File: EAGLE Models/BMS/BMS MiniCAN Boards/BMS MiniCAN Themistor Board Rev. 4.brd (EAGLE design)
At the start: 150.2 x 63.2 mm, 112 parts, among them IC1 AT90CAN128, IC2 MCP2551SO8, IC3 NUP2105L, U1 0ZCH0050FF2G

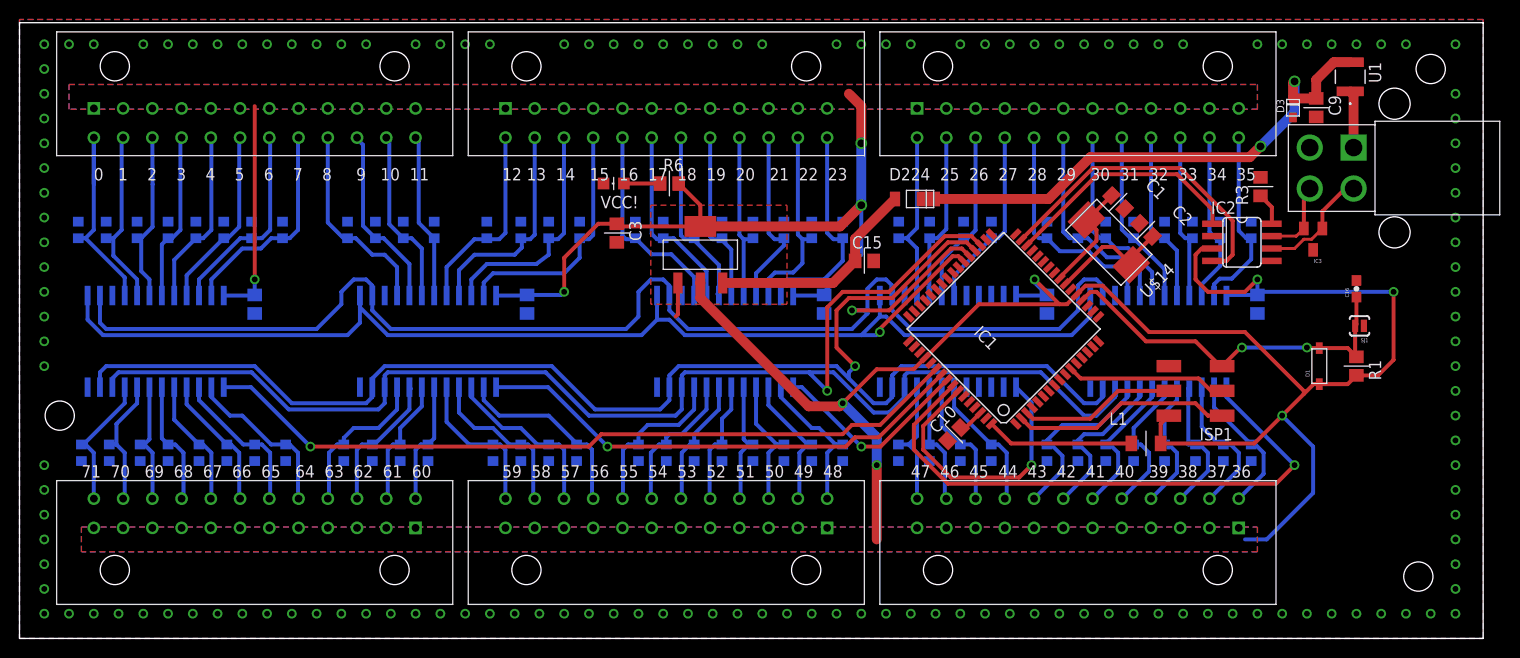
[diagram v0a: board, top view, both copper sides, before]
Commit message: Fixed silkscreens and crystal
Fixed the silkscreens and replaced crystal.
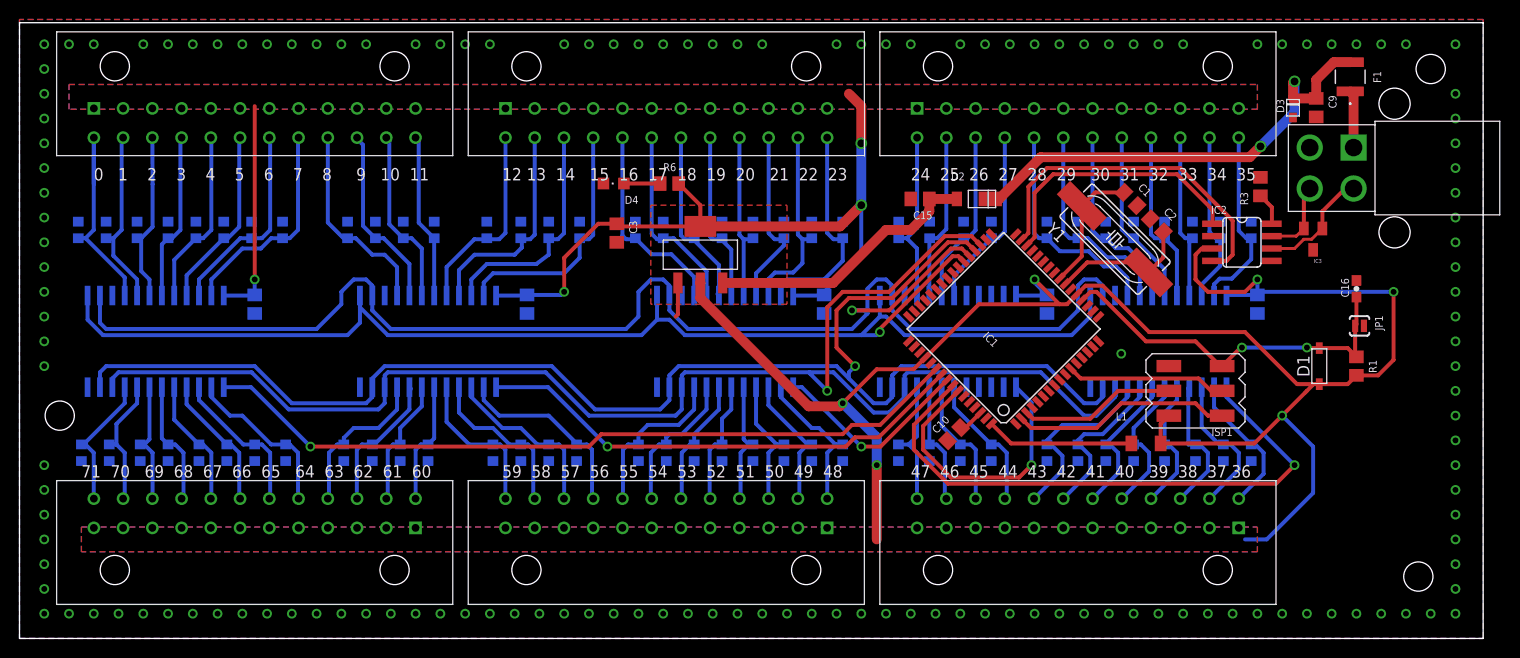
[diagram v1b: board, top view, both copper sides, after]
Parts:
- removed U$14: AX-16.000MBGE-T, BMS Lbr:2-SMD_NO_LEAD_(DFN_LCC)
- added Y1: 16M, SparkFun-FreqCtrl:HC49UP
- moved C15 8.54 mm to (92.4, 43.8), turned to 180 degrees
- moved D2 6.35 mm to (98.7, 43.8)
- moved C1 1.31 mm to (114.0, 43.8)
- moved C2 1.21 mm to (116.7, 41.1)
- renumbered SJ1 to JP1, U$1 to IC4, U$10 to X4, U$11 to X5, U$12 to X6, U$13 to X7, U$2 to X1, U$3 to X2, U$5 to IC5, U$6 to IC6, U$7 to IC7, U$8 to IC8, U$9 to X3, U1 to F1, VCC! to D4
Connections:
- net XTAL1: now also Y1.1; no longer U$14.P$1
- net XTAL2: now also Y1.2; no longer U$14.P$2
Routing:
- net 12V: track 54.7 -> 48.4 mm
- net 12VIN: track 22.6 -> 28.3 mm
- net RXCAN: track 32.8 -> 35.6 mm
- net TXCAN: track 25.0 -> 27.7 mm
- net XTAL2: track 12.9 -> 14.7 mm
- net XTAL1: track 11.6 -> 13.2 mm
- net GND: vias 146 -> 147

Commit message: Fixed resistor values
Fixed resistor values.
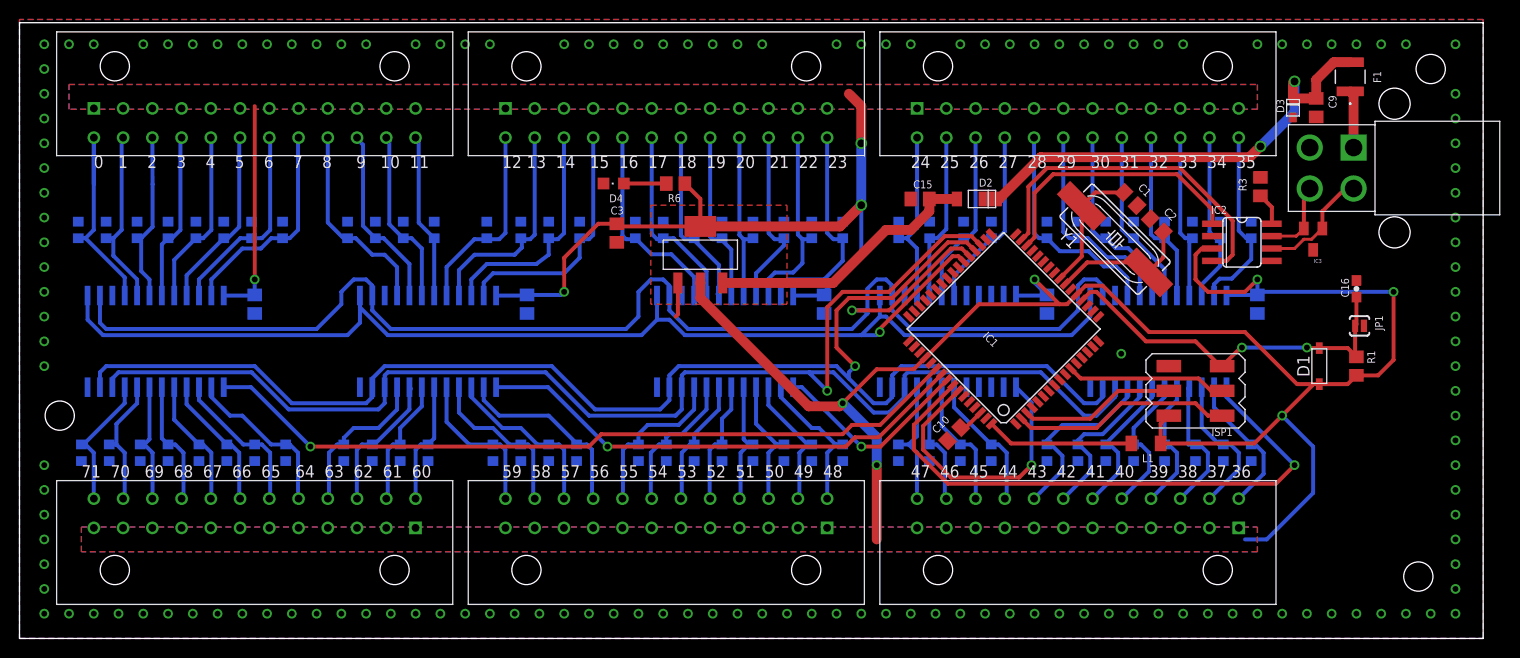
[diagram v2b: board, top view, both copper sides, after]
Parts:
- R10, R11, R12, R13, R14, R15, R16, R17, R18, R19, R20, R21, R22, R23, R24, R25, R26, R27, R28, R29, R30, R31, R32, R33, R34, R35, R36, R37, R38, R39, R4, R40, R41, R42, R43, R44, R45, R46, R47, R48, R49, R5, R50, R51, R52, R53, R54, R55, R56, R57, R58, R59, R60, R61, R62, R63, R64, R65, R66, R67, R68, R69, R70, R71, R72, R73, R74, R75, R76, R77, R78, R79: value (none) -> 10K
- moved R6 0.64 mm to (67.3, 45.4)
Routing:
- net N$9: track 3.71 -> 4.35 mm
